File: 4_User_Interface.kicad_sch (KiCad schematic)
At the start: 37 parts, among them J40 OLED_I2C, SW1 Accelerate, SW2 Decelerate, SW3 Left, SW4 Right, SW5 Home, SW6 EStop

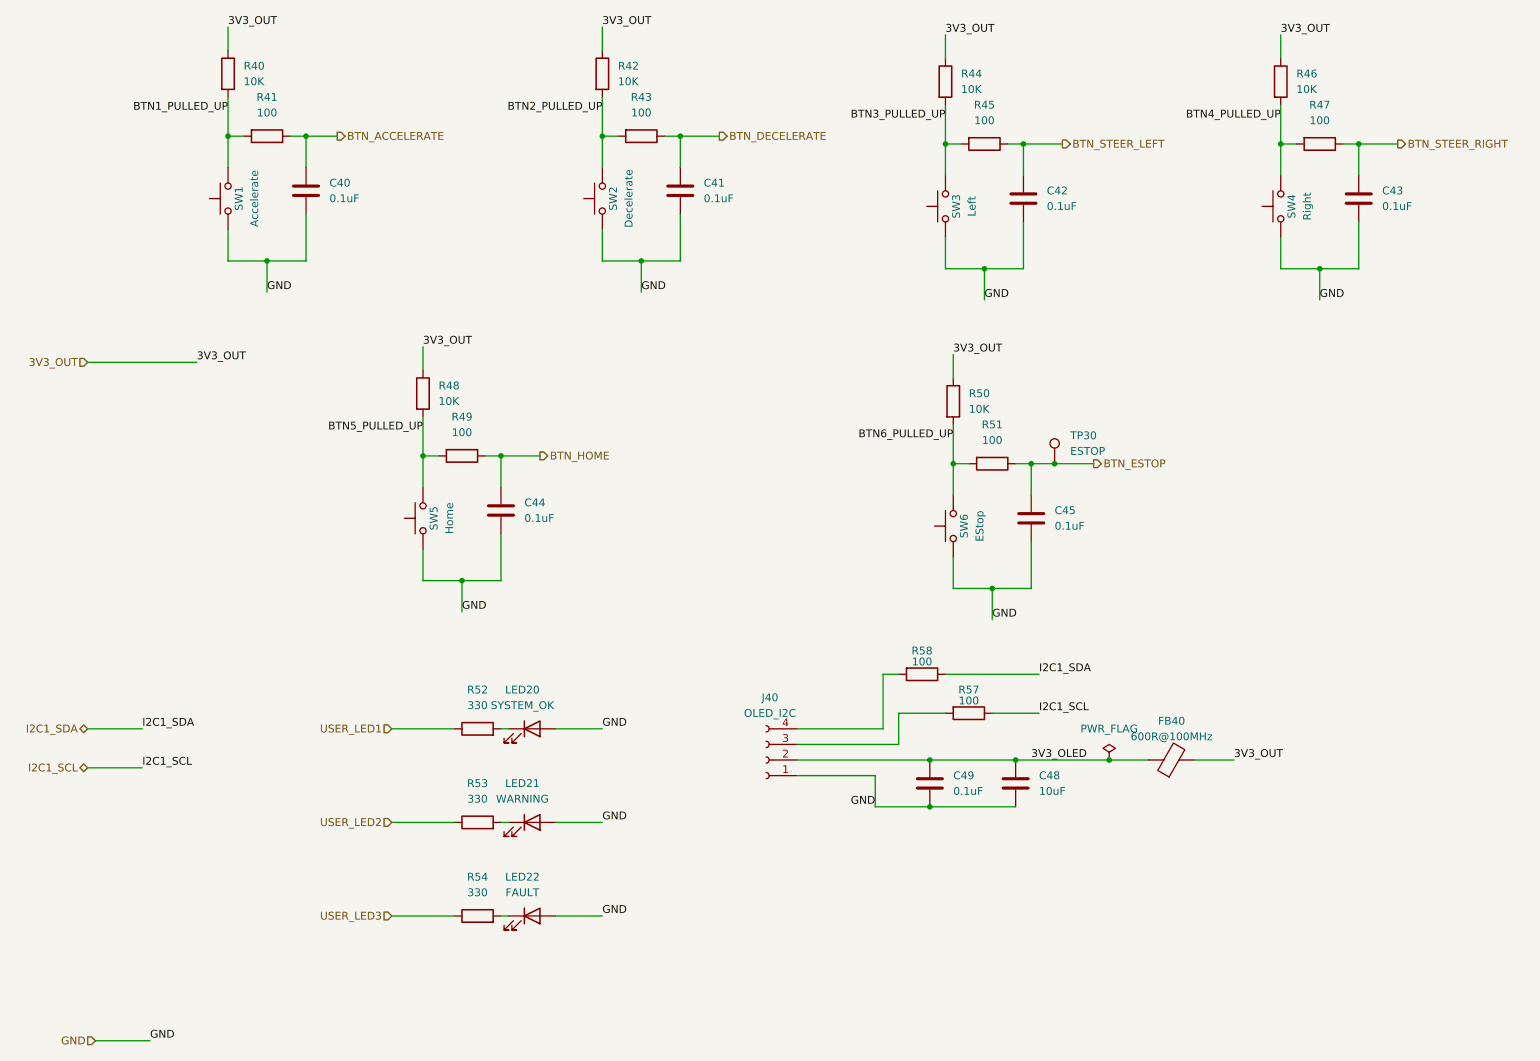
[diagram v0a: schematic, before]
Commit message: Updated BOM. Initial review and corrections
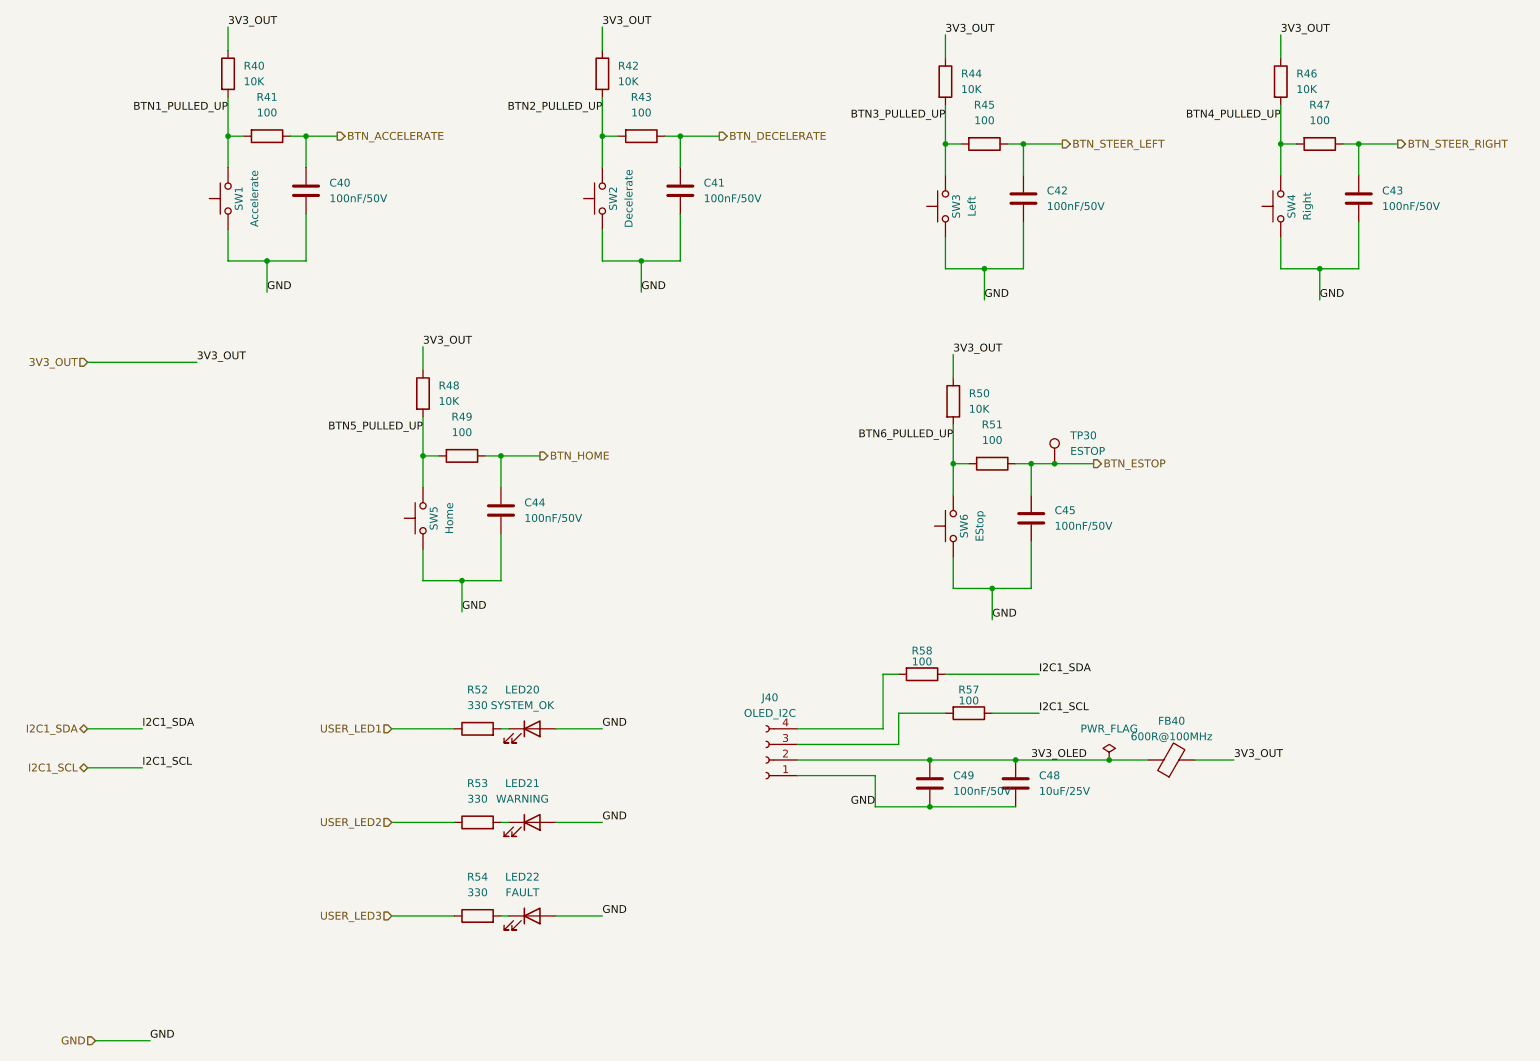
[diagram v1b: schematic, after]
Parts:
- C40, C41, C42, C43, C44, C45, C49: value 0.1uF -> 100nF/50V; LCSC C1848 -> C6119867
- C48: value 10uF -> 10uF/25V; LCSC C13585 -> C6119815
- FB40: LCSC C1016 -> C16902
- J40, TP30: now left out of the parts list
- LED20: LCSC C72043 -> C434439
- LED21: LCSC C72038 -> C264322
- LED22: LCSC C72041 -> C559117
- R40, R42, R44, R46, R48, R50: LCSC C17902 -> C15401
- R41: LCSC 17901 -> C22775
- R43, R45, R47, R49, R51, R58: LCSC C17901 -> C22775
- R52, R53, R54: LCSC C17630 -> C22104
- R57: LCSC (none) -> C22775

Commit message: Cleaned up schematic. Added mounting holes.
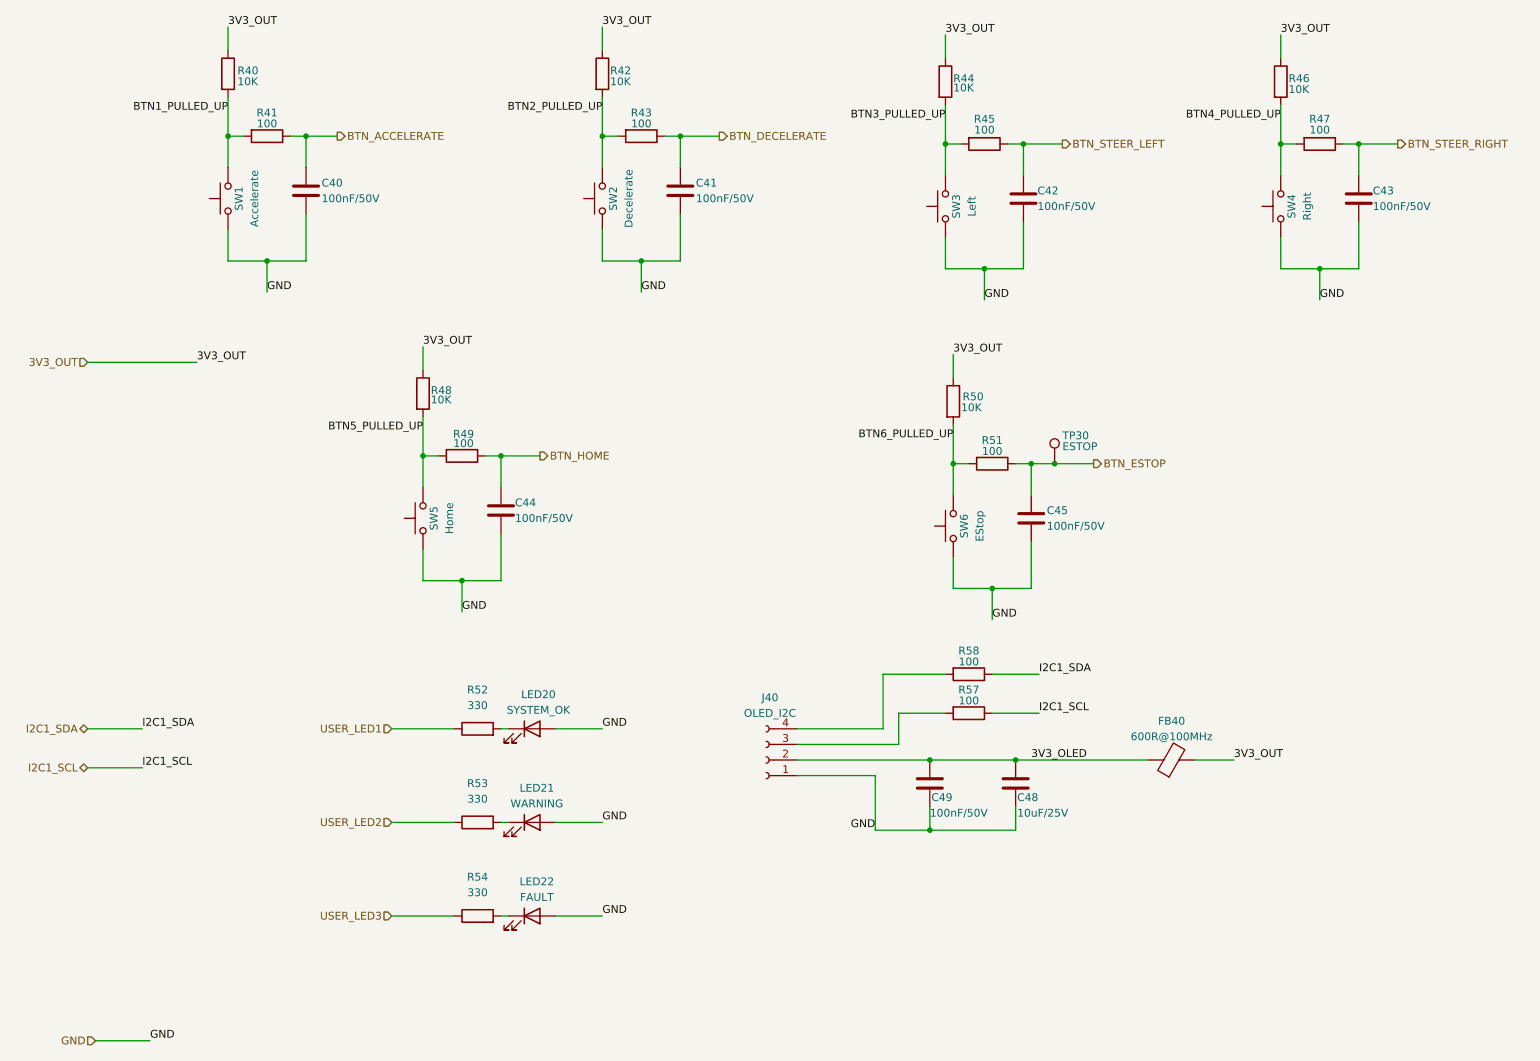
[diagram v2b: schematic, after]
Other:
- moved on the sheet: R58
